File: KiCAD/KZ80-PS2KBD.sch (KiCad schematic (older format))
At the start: 23 parts, among them J1 232C(DEBUG), J2 PS/2 KB, J3 SBC8080 BUS, J4 ADR-JP2, J5 ADR-JP1, J6 ICSP, J7 CON-A, U1 74HC139, U2 74HC00, U3 8255, U4 ATmega328P-PU

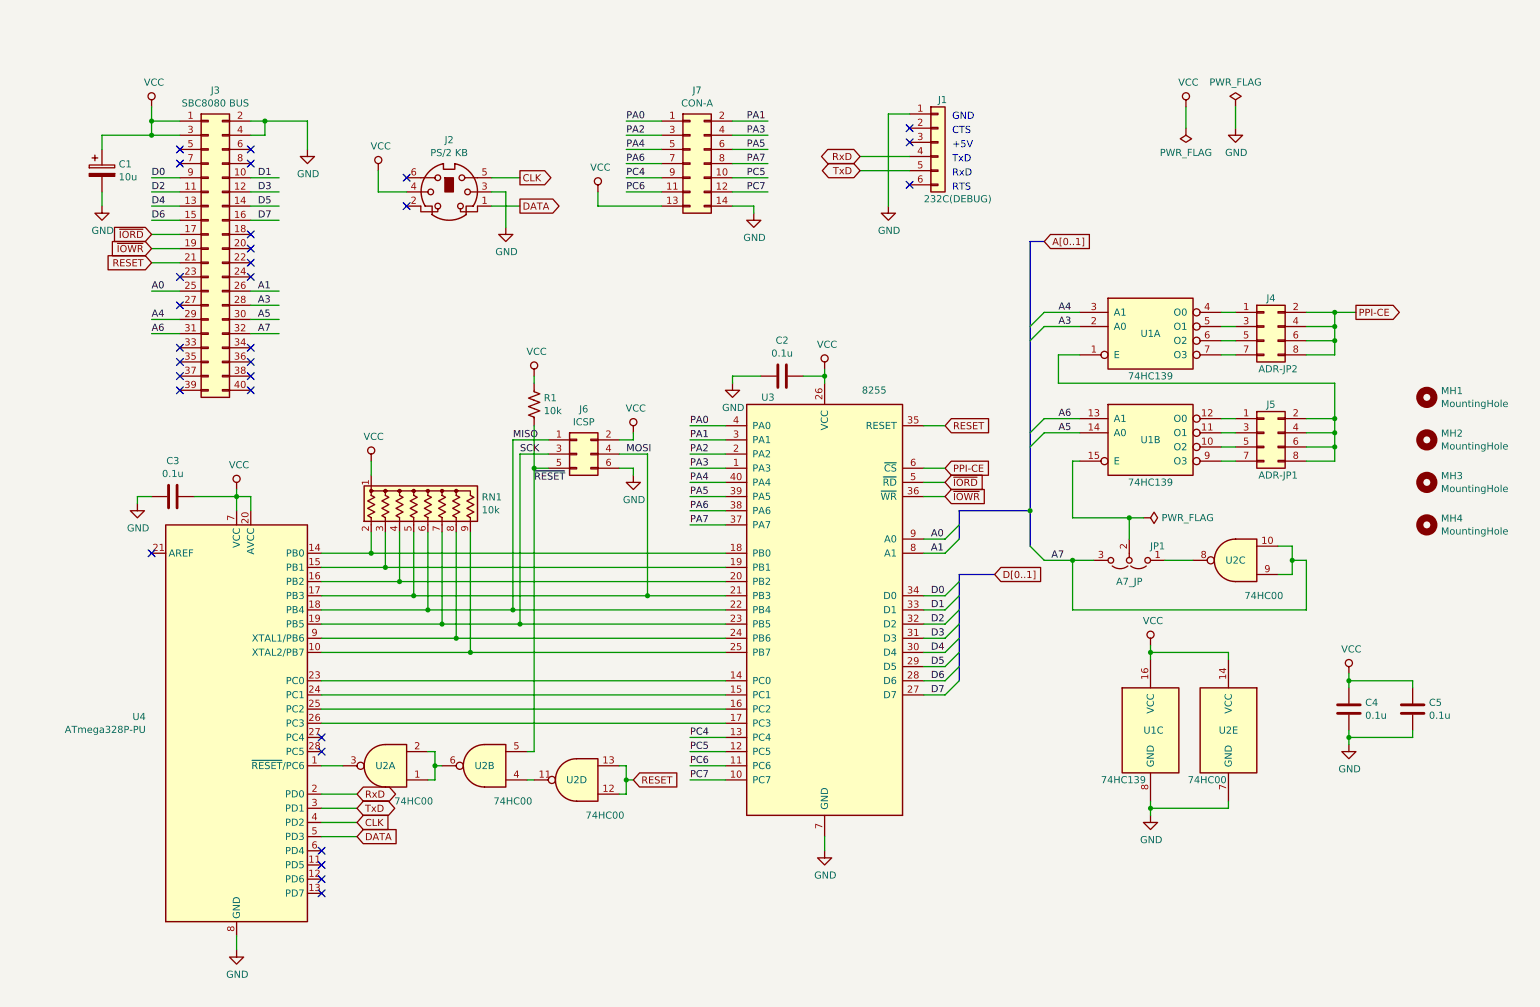
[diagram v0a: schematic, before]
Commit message: CMT出力回路追加・REV2基板ガーバー出力
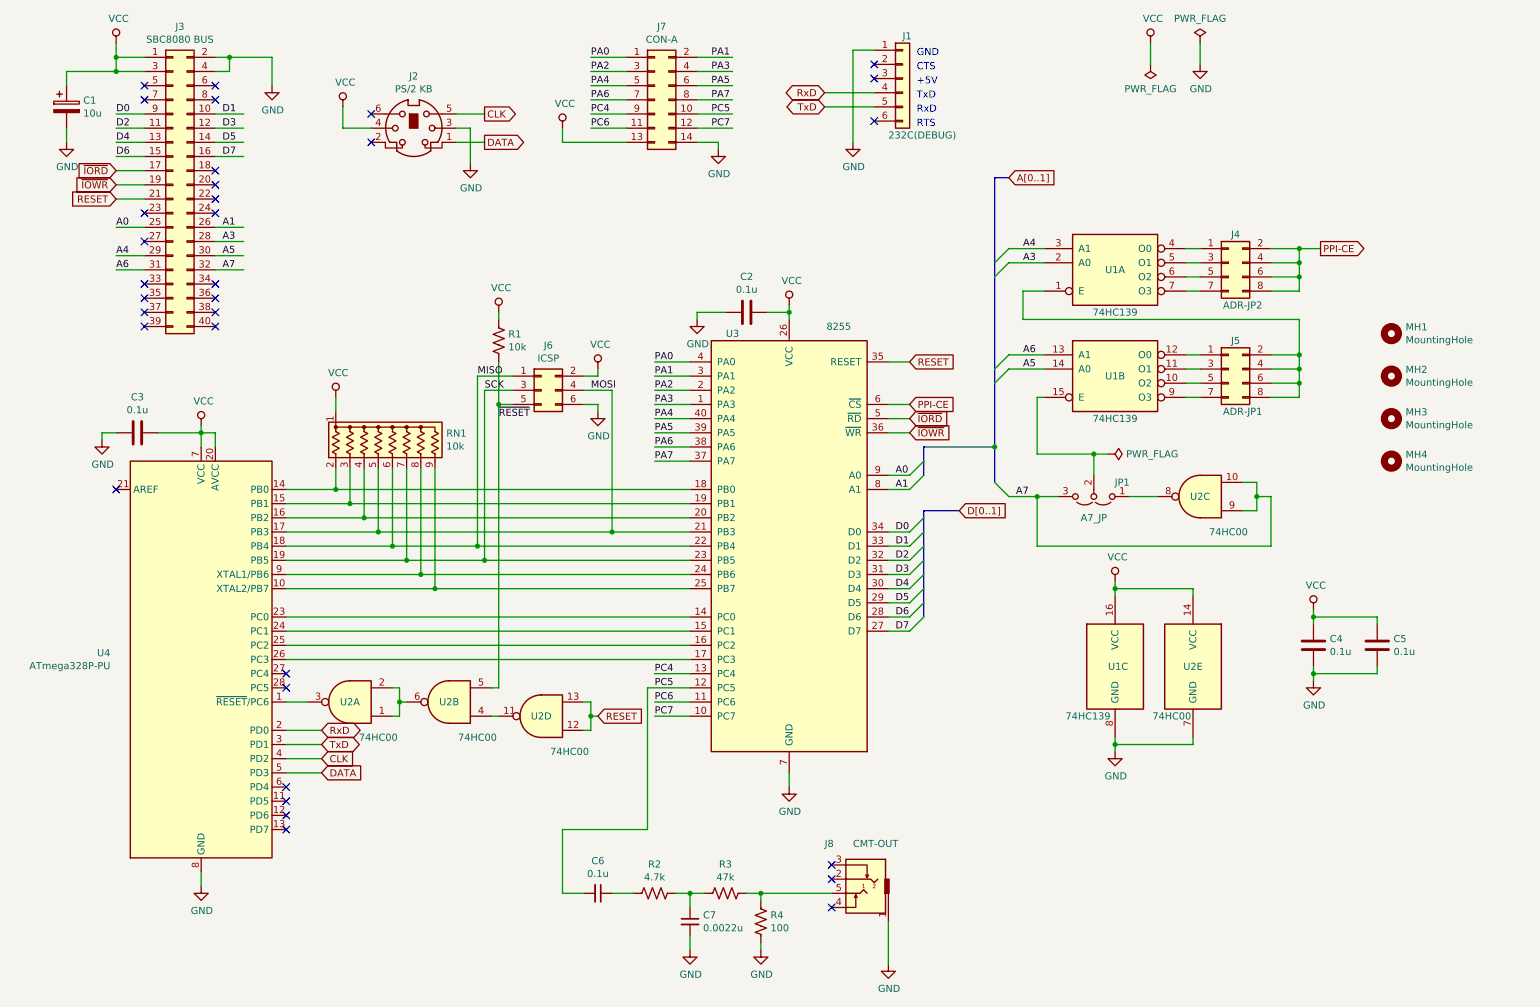
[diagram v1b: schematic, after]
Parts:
- added C6: 0.1u, Capacitor_THT:C_Disc_D3.0mm_W1.6mm_P2.50mm, symbol Device:C_Small
- added C7: 0.0022u, Capacitor_THT:C_Disc_D3.0mm_W1.6mm_P2.50mm, symbol Device:C_Small
- added J8: CMT-OUT, AJ-1780:AJ-1780, symbol AJ-1780:Audio-Jack-3_2Switches
- added R2: 4.7k, Resistor_THT:R_Axial_DIN0207_L6.3mm_D2.5mm_P10.16mm_Horizontal, symbol Device:R_US
- added R3: 47k, Resistor_THT:R_Axial_DIN0207_L6.3mm_D2.5mm_P10.16mm_Horizontal, symbol Device:R_US
- added R4: 100, Resistor_THT:R_Axial_DIN0207_L6.3mm_D2.5mm_P10.16mm_Horizontal, symbol Device:R_US
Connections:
- wire segments 224 -> 238
- no-connect marks 30 -> 33
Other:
- moved on the sheet: C1, C2, C3, C4, C5, J1, J2, J3, J4, J5, J6, J7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
